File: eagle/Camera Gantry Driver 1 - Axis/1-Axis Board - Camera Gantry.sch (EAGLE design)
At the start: 43 parts, among them IC1 DRV8312A, U1 PTN78000, U2 DSPIC33FJ802GP-28, U3 LP2950-3.3ACZ

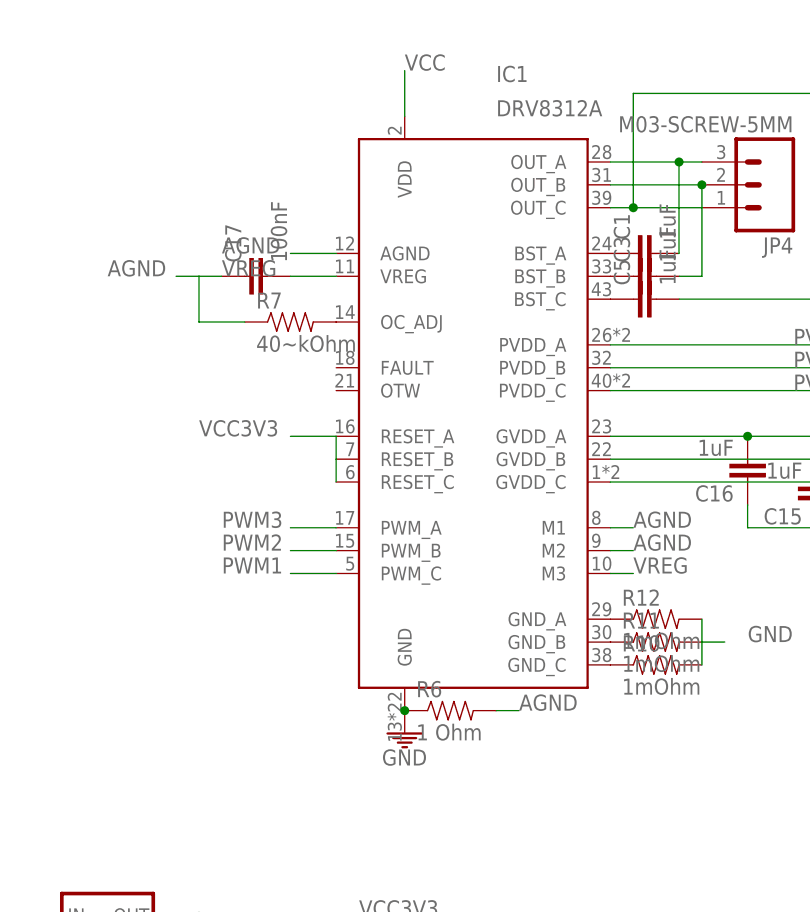
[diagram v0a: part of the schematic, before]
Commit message: Finished 1-Axis Dev for Camera Stab.
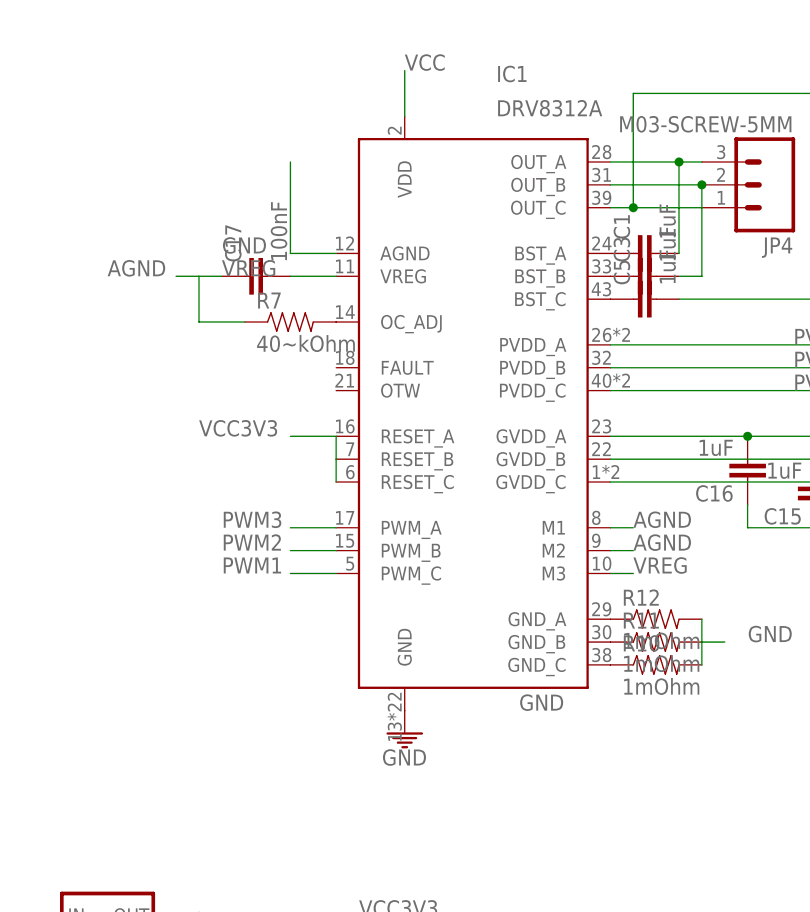
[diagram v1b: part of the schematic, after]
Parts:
- removed R6: 1 Ohm, ASL:RESISTOR0805-RES
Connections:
- net AGND: no longer IC1.AGND, R6.2
- net GND: now also IC1.AGND; no longer R6.1
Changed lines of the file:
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@@
 <part name="U3" library="ASL" deviceset="LP2950" device="ACZ" technology="-3.3"/>
 <part name="C2" library="ASL" deviceset="CAP" device="1206" value="2.2uF"/>
-<part name="R6" library="ASL" deviceset="RESISTOR" device="0805-RES" value="1 Ohm"/>
 <part name="R10" library="ASL" deviceset="RESISTOR" device="1206" value="1mOhm"/>
 <part name="R11" library="ASL" deviceset="RESISTOR" device="1206" value="1mOhm"/>
@@
 <instance part="U3" gate="G$1" x="154.94" y="38.1"/>
 <instance part="C2" gate="G$1" x="165.1" y="33.02"/>
-<instance part="R6" gate="G$1" x="193.04" y="60.96"/>
 <instance part="R10" gate="G$1" x="215.9" y="66.04"/>
 <instance part="R11" gate="G$1" x="215.9" y="68.58"/>
@@
 <pinref part="IC1" gate="G$1" pin="GND"/>
 <pinref part="GND5" gate="1" pin="GND"/>
-<pinref part="R6" gate="G$1" pin="1"/>
-<junction x="187.96" y="60.96"/>
-<pinref part="R6" gate="G$1" pin="1"/>
+<label x="200.66" y="60.96" size="1.778" layer="95"/>
 </segment>
 <segment>
@@
 <wire x1="241.3" y1="78.74" x2="241.3" y2="76.2" width="0.2032" layer="91"/>
 <pinref part="GND8" gate="1" pin="GND"/>
+</segment>
+<segment>
+<pinref part="IC1" gate="G$1" pin="AGND"/>
+<wire x1="180.34" y1="111.76" x2="175.26" y2="111.76" width="0.2032" layer="91"/>
+<label x="167.64" y="111.76" size="1.778" layer="95"/>
+<wire x1="175.26" y1="111.76" x2="175.26" y2="121.92" width="0.2032" layer="91"/>
 </segment>
 </net>
@@
 <net name="AGND" class="0">
 <segment>
-<pinref part="IC1" gate="G$1" pin="AGND"/>
-<wire x1="180.34" y1="111.76" x2="175.26" y2="111.76" width="0.2032" layer="91"/>
-<label x="167.64" y="111.76" size="1.778" layer="95"/>
-</segment>
-<segment>
-<pinref part="R6" gate="G$1" pin="2"/>
-<wire x1="198.12" y1="60.96" x2="200.66" y2="60.96" width="0.2032" layer="91"/>
-<label x="200.66" y="60.96" size="1.778" layer="95"/>
-</segment>
-<segment>
 <pinref part="IC1" gate="G$1" pin="M1"/>

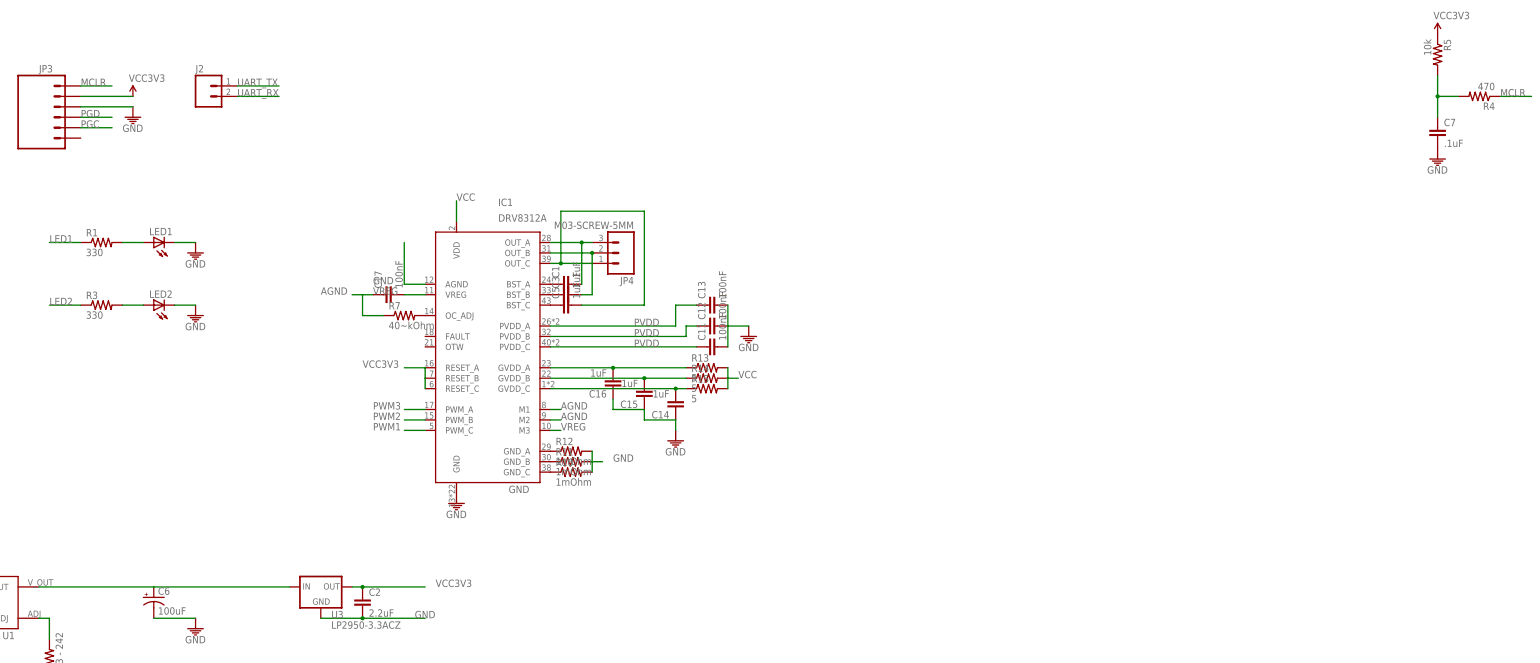
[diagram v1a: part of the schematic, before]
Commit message: Added some filtering to the 1-Axis Gantry Board
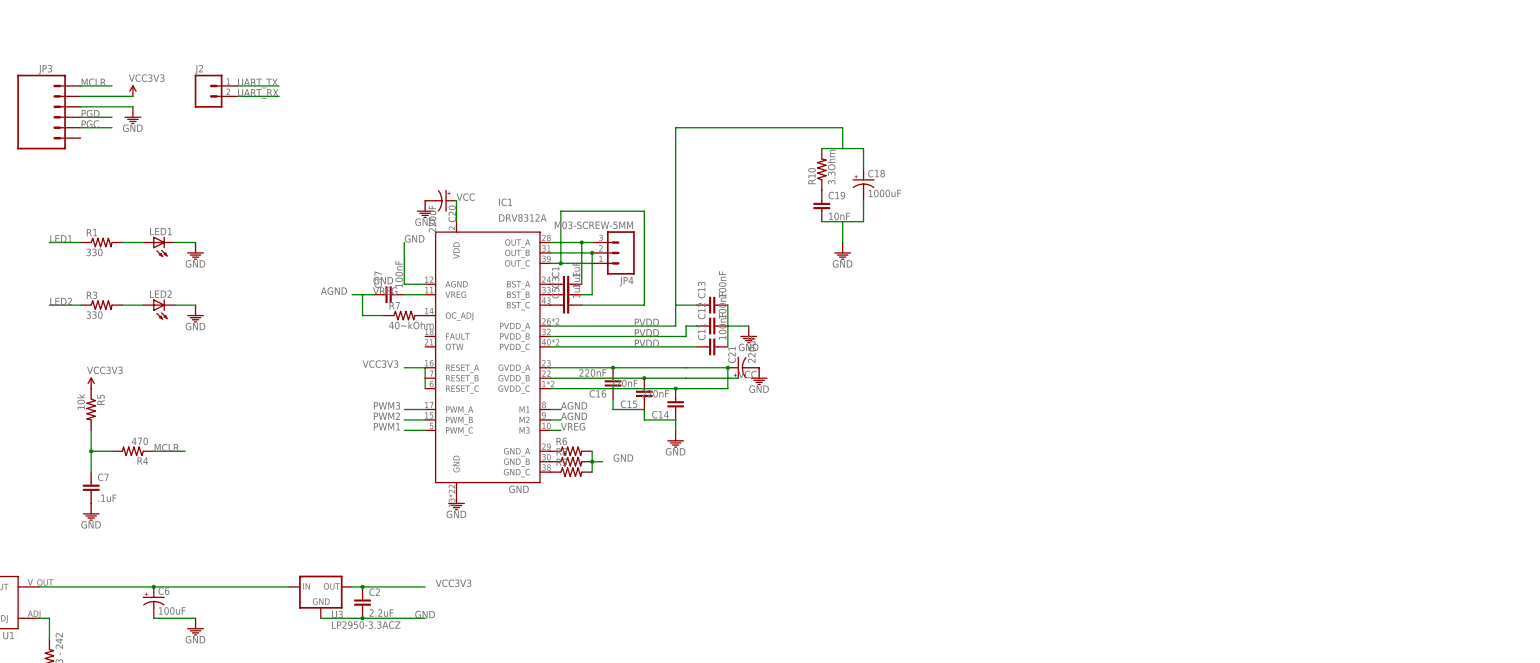
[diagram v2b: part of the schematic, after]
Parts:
- removed R11, R12: 1mOhm, ASL:RESISTOR1206
- removed R13, R14, R15: 5, ASL:RESISTOR0805-RES
- added C18: 1000uF, ASL:CAP_POLPTH4
- added C19: 10nF, ASL:CAP1206
- added C20, C21: 220uF, ASL:CAP_POLPTH1
- added R6, R8, R9: (no value), pavlo:RESISTOR
- C14, C15, C16: value 1uF -> 220nF
- C6: device CMPE118lib:CAP_POL -> ASL:CAP_POLPTH1
- R10: value 1mOhm -> 3.3Ohm; device ASL:RESISTOR1206 -> ASL:RESISTOR0805-RES
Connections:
- removed net N$14: C15.2, IC1.GVDD_B, R14.1
- removed net N$16: C14.2, IC1.GVDD_C, R15.1
- net GND: now also C18.-, C19.2, C20.-, C21.-, R6.2, R8.2, R9.2; no longer R10.2, R11.2, R12.2
- net N$11: now also R8.1; no longer R11.1
- net N$12: now also IC1.GND_C, R9.1; no longer IC1.GND_A, R12.1
- net N$13: now also C19.1, R10.1; no longer C16.2, IC1.GVDD_A, R13.1
- net N$9: now also IC1.GND_A, R6.1; no longer IC1.GND_C, R10.1
- net PVDD: now also C18.+, R10.2
- net VCC: now also C14.2, C15.2, C16.2, C20.+, C21.+, IC1.GVDD_A, IC1.GVDD_B, IC1.GVDD_C; no longer R13.2, R14.2, R15.2
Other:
- moved on the sheet: C7, R10, R4, R5

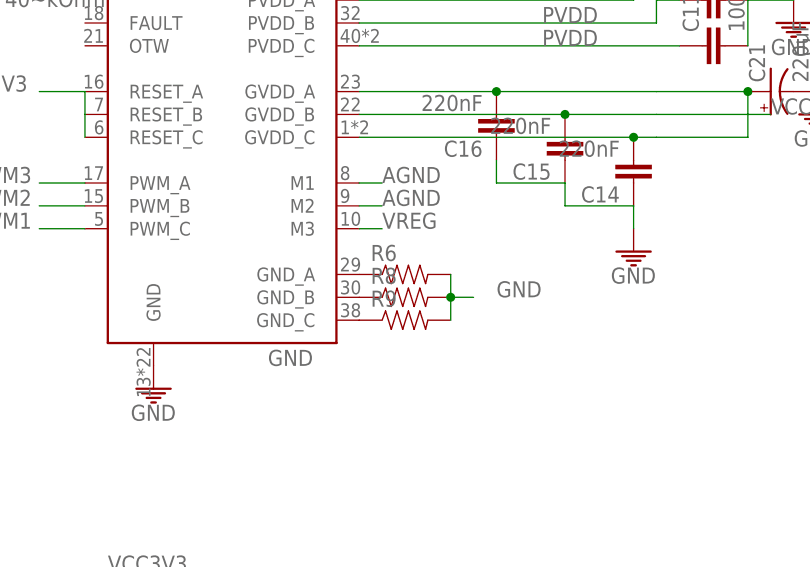
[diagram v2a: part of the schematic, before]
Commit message: Updating libraries and DRV83x2 related boards.
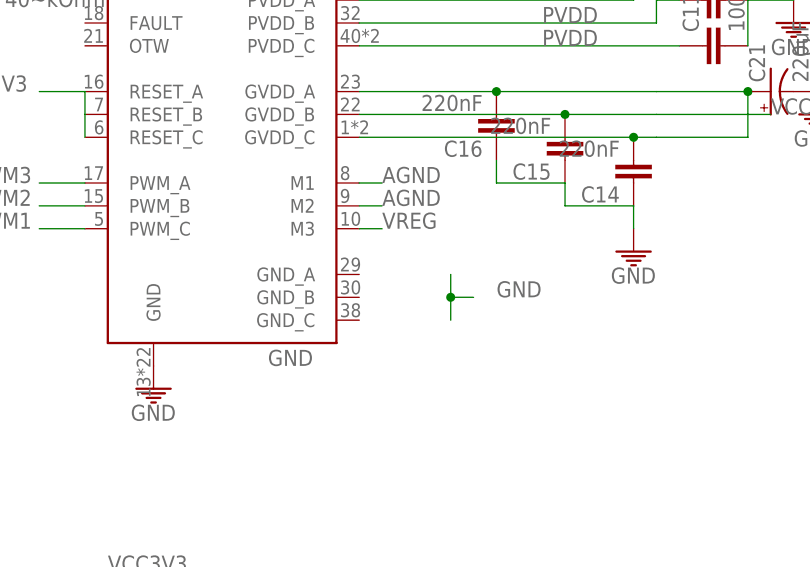
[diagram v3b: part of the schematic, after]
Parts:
- removed R6, R8, R9: (no value), pavlo:RESISTOR
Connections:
- removed net N$11: IC1.GND_B, R8.1
- removed net N$12: IC1.GND_C, R9.1
- removed net N$9: IC1.GND_A, R6.1
- net GND: no longer R6.2, R8.2, R9.2
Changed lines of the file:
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@@
 <?xml version="1.0" encoding="utf-8"?>
 <!DOCTYPE eagle SYSTEM "eagle.dtd">
-<eagle version="6.2">
+<eagle version="6.5.0">
 <drawing>
 <settings>
@@
 <part name="GND8" library="ASL" deviceset="GND" device=""/>
 <part name="C17" library="ASL" deviceset="CAP" device="1206" value="100nF"/>
-<part name="R6" library="pavlo" deviceset="RESISTOR" device=""/>
-<part name="R8" library="pavlo" deviceset="RESISTOR" device=""/>
-<part name="R9" library="pavlo" deviceset="RESISTOR" device=""/>
 <part name="C18" library="ASL" deviceset="CAP_POL" device="PTH4" value="1000uF"/>
 <part name="C19" library="ASL" deviceset="CAP" device="1206" value="10nF"/>
@@
 <instance part="GND8" gate="1" x="241.3" y="73.66"/>
 <instance part="C17" gate="G$1" x="172.72" y="109.22" rot="R90"/>
-<instance part="R6" gate="G$1" x="215.9" y="71.12"/>
-<instance part="R8" gate="G$1" x="215.9" y="68.58"/>
-<instance part="R9" gate="G$1" x="215.9" y="66.04"/>
 <instance part="C18" gate="G$1" x="287.02" y="137.16"/>
 <instance part="C19" gate="G$1" x="276.86" y="129.54"/>
@@
 <wire x1="220.98" y1="68.58" x2="223.52" y2="68.58" width="0.2032" layer="91"/>
 <label x="226.06" y="68.58" size="1.778" layer="95"/>
-<pinref part="R6" gate="G$1" pin="2"/>
-<pinref part="R8" gate="G$1" pin="2"/>
 <junction x="220.98" y="68.58"/>
-<pinref part="R9" gate="G$1" pin="2"/>
 </segment>
 <segment>
@@
 </segment>
 </net>
-<net name="N$9" class="0">
-<segment>
-<pinref part="IC1" gate="G$1" pin="GND_A"/>
-<pinref part="R6" gate="G$1" pin="1"/>
-</segment>
-</net>
-<net name="N$11" class="0">
-<segment>
-<pinref part="IC1" gate="G$1" pin="GND_B"/>
-<pinref part="R8" gate="G$1" pin="1"/>
-</segment>
-</net>
-<net name="N$12" class="0">
-<segment>
-<pinref part="IC1" gate="G$1" pin="GND_C"/>
-<pinref part="R9" gate="G$1" pin="1"/>
-</segment>
-</net>

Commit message: More motor driver refactoring.
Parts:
- removed D1: DIODE-SCHOTTKY240A, CMPE118lib:DIODE-SCHOTTKY240A
- removed IC1: DRV8312A, pavlo:DRV8312A
- removed J2: (no value), ASL:M02PTH
- added C22, C23: .1uF, ASL:CAP0805
- added C24: 1.6nF, ASL:CAP0805
- added C25: 10uF 16V, ASL:CAP1206
- added C26: 1uF 16V, CMPE118lib:CAP1206
- added C27: .1uF, CMPE118lib:CAP1206
- added C28: 10uF, ASL:CAP1206
- added D5: PMEG2010AEH, DRV83x2Support:PMEG2010AEH
- added L6: LQM31PN3R3M00L, DRV83x2Support:LQM31PN3R3M00L
- added R11: 158k, ASL:RESISTOR0805-RES
- added R6: OC_ADJ, ASL:RESISTOR0805-RES
- added R8: 47k, ASL:RESISTOR0805-RES
- added R9: 18.2k, ASL:RESISTOR0805-RES
- added SL1: (no value), ASL:M04LOCK
- added U$1: DSPIC33EP256MC506, DRV83x2Support:DSPIC33EP256MC506
- added U$2, U$3, U$4: ERJ-8BWJR010V, DRV83x2Support:ERJ-8BWJR010V
- C1, C3, C5: value 1uF -> .1uF; device ASL:CAP1206 -> CMPE118lib:CAP1206
- C11: value 100nF -> 330uF; device ASL:CAP1206 -> ASL:CAP_POLPTH4
- C12: device ASL:CAP1206 -> ASL:CAP0805
- C13: value 100nF -> 47uF; device ASL:CAP1206 -> ASL:CAP_POLPTH4
- C14, C15: value 220nF -> 1uF; device ASL:CAP1206 -> ASL:CAP0805
- C16: value 220nF -> .1uF; device ASL:CAP1206 -> ASL:CAP0805
- C17: value 100nF -> .1uF; device ASL:CAP1206 -> ASL:CAP0805
- C2: value 2.2uF -> .1uF; device ASL:CAP1206 -> CMPE118lib:CAP1206
- C20, C21: value 220uF -> .1uF; device ASL:CAP_POLPTH1 -> ASL:CAP0805
- C8: value 10uF -> 1uF; device CMPE118lib:CAP1206 -> ASL:CAP0805
- C9: value .1uF -> 1uF; device CMPE118lib:CAP1206 -> ASL:CAP0805
- JP1, JP2: value M03PTH -> (none); device ASL:M03PTH -> ASL:M06LOCK
- JP4: value M03-SCREW-5MM -> (none); device ASL:M03-SCREW-5MM -> ASL:M06LOCK
- R7: value 40~kOhm -> 1
- U2: value DSPIC33FJ802GP-28 -> DRV8312_DDW_44; device CMPE118lib:DSPIC33FJ802GP-28 -> DRV83x2Support:DRV8312_DDW_44
- U3: value LP2950-3.3ACZ -> TPS61085_DGK_8; device ASL:LP2950-3.3ACZ -> DRV83x2Support:TPS61085_DGK_8
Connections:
- removed net AGND: C17.1, IC1.M1, IC1.M2, R7.1
- removed net CAN_RX: U2.RB4
- removed net CAN_TX: U2.RB7
- removed net N$18: C3.1, IC1.BST_B
- removed net PWM1: IC1.PWM_C, U2.RB14
- removed net PWM2: IC1.PWM_B, U2.RB12
- removed net PWM3: IC1.PWM_A, U2.RB10
- removed net RA0: U2.RA0
- removed net RA2: U2.RA2
- removed net RB0: U2.RB0
- removed net RB1: U2.RB1
- removed net RB15: U2.RB15
- removed net RB2: U2.RB2
- removed net RB9: U2.RB9
- removed net TEMP: U2.RA1
- removed net UART_RX: J2.1, U2.RB13
- removed net UART_TX: J2.2, U2.RB11
- removed net VREG: C17.2, IC1.M3, IC1.VREG
- removed net V_SENSE: U2.RB3
- new net FAULT: U$1.RPI119/RG7, U2.*FAULT
- new net GVDD: C11.+, C13.+, C14.1, C15.1, C8.2, C9.2, D5.C, L6.2, R11.1, U2.GVDD_A, U2.GVDD_B, U2.GVDD_C, U2.GVDD_C_2, U2.VDD
- new net N$11: R8.1, U3.COMP
- new net N$12: C24.2, R8.2
- new net N$14: C28.1, U$1.VCAP
- new net N$16: R11.2, R9.1, U3.FB
- new net N$21: C16.2, U2.BST_C
- new net N$22: JP2.6, U$1.PGEC2/ASCL2/RP38/RB6
- new net N$23: JP1.1, U$1.RP39/INT0/RB7
- new net N$24: JP1.2, U$1.TMS/ASDA1/RP41/RB9
- new net N$25: JP1.3, U$1.RP54/RC6
- new net N$27: JP1.5, U$1.RP56/RC8
- new net N$28: JP1.6, U$1.RP97/RF1
- new net N$29: JP2.2, U$1.RP120/RG8
- new net N$30: C17.2, U2.BST_B
- new net N$32: JP1.4, U$1.RP55/RC7
- new net N$35: JP4.4, U$1.SCK1/RPI51/RC3
- new net N$36: JP4.5, U$1.SDA1/RPI52/RC4
- new net N$37: JP4.6, U$1.SCL1/RPI53/RC5
- new net N$38: JP4.3, U$1.SDI1/RPI25/RA9
- new net N$39: C20.1, U2.BST_A
- new net N$40: SL1.1, U$1.PGED3/VREF-/AN2/C2IN1-/*SS1/RPI32/CTED2/RB0
- new net N$41: SL1.2, U$1.AN1/C2IN1+/RA1
- new net N$42: SL1.3, U$1.AN0/OA2OUT/RA0
- new net N$43: SL1.4, U$1.AN9/RPI27/RA11
- new net N$44: JP4.2, U$1.CVREF2O/SDO1/RP20/T1CK/RA4
- new net N$45: C12.2, R6.1, R7.1, U2.AGND, U2.M1, U2.M2
- new net N$47: C12.1, U2.M3, U2.VREG
- new net N$9: C1.2, U$1.AVSS
- new net OC_ADJ: R6.2, U2.OC_ADJ
- new net OTW: U$1.TDI/RA7, U2.*OTW
- new net OUT_A: C20.2, U2.OUT_A
- new net OUT_B: C17.1, U2.OUT_B
- new net OUT_C: C16.1, U2.OUT_C
- new net PWM_A: U$1.RPI46/PWM1H/T3CK/RB14, U2.PWM_A
- new net PWM_B: U$1.RPI44/PWM2H/RB12, U2.PWM_B
- new net PWM_C: U$1.RP42/PWM3H/RB10, U2.PWM_C
- new net RESET_A: U$1.RPI47/PWM1L/T5CK/RB15, U2.*RESET_A
- new net RESET_B: U$1.RPI45/PWM2L/CTPLS/RB13, U2.*RESET_B
- new net RESET_C: U$1.RB43/PWM3L/RB11, U2.*RESET_C
- net GND: now also C10.1, C11.-, C13.-, C14.2, C15.2, C2.1, C21.2, C22.2, C23.2, C24.1, C25.1, C26.2, C27.2, C28.2, C3.1, C5.2, C8.1, C9.1, JP4.1, R7.2, R9.2, U$1.VSS, U$1.VSS_2, U$1.VSS_3, U$2.2, U$3.2, U$4.2, U2.EPAD, U2.GND, U2.GND_2, U2.GND_3, U3.PGND; no longer C10.2, C11.2, C12.2, C13.2, C14.1, C15.1, C16.1, C2.2, C20.-, C21.-, C8.2, C9.2, IC1.AGND, IC1.GND, JP1.3, U2.AVSS, U2.VSS@19, U2.VSS@8, U3.GND
- net LED1: now also U$1.AN7/C3IN1-/C4IN1-/RC1; no longer U2.RA3
- net LED2: now also U$1.AN8/C3IN1+/*U1RTS/BCLK1/FLT3/RC2; no longer U2.RA4
- net MCLR: now also U$1.*MCLR; no longer U2.MCLR
- net N$10: now also C27.1, U3.SS; no longer C5.2, IC1.OUT_C, JP4.1
- net N$15: now also D5.A, U3.SW; no longer U2.RB8
- net N$17: now also JP2.1, U$1.RP118/RG6; no longer C1.1, IC1.BST_A
- net N$19: now also JP2.4, U$1.FLT32/SCL2/RP36/RB4; no longer C5.1, IC1.BST_C
- net N$20: now also JP2.5, U$1.PGED2/ASDA2/RP37/RB5; no longer IC1.OC_ADJ, R7.2
- net N$4: now also U$2.1, U2.GND_C; no longer C1.2, IC1.OUT_A, JP4.3
- net N$5: now also U$3.1, U2.GND_A; no longer C3.2, IC1.OUT_B, JP4.2
- net N$7: now also U$4.1, U2.GND_B; no longer C8.1, U2.VCAP
- net N$8: now also C1.1, U$1.AVDD; no longer C4.1, D1.C, U1.V_IN
- net PGC: now also U$1.PGEC1/AN4/C1IN1+/RPI34/RB2; no longer U2.RB6
- net PGD: now also U$1.PGED1/AN5/C1IN1-/RP35/RB3; no longer U2.RB5
- net PVDD: now also C21.1, C22.1, C23.1, C4.1, U1.V_IN, U2.PVDD_A, U2.PVDD_A_2, U2.PVDD_B, U2.PVDD_C, U2.PVDD_C_2; no longer C11.1, C12.1, C13.1, D1.A, IC1.PVDD_A, IC1.PVDD_B, IC1.PVDD_C
- net VCC: now also C10.2, C2.2, C25.2, C26.1, C3.2, C5.1, L6.1, U$1.VDD, U$1.VDD_2, U$1.VDD_3, U$1.VDD_4, U3.EN, U3.FREQ; no longer C14.2, C15.2, C16.2, C20.+, C21.+, IC1.GVDD_A, IC1.GVDD_B, IC1.GVDD_C, IC1.VDD, JP1.1, JP1.2
- net VCC3V3: no longer C10.1, C2.1, C9.1, IC1.RESET_A, IC1.RESET_B, IC1.RESET_C, JP2.1, JP2.2, U2.AVDD, U2.VDD, U3.OUT
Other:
- moved on the sheet: C1, C10, C12, C14, C15, C16, C17, C2, C3, C5, C6, C8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
